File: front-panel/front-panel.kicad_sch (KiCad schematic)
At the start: 9 parts

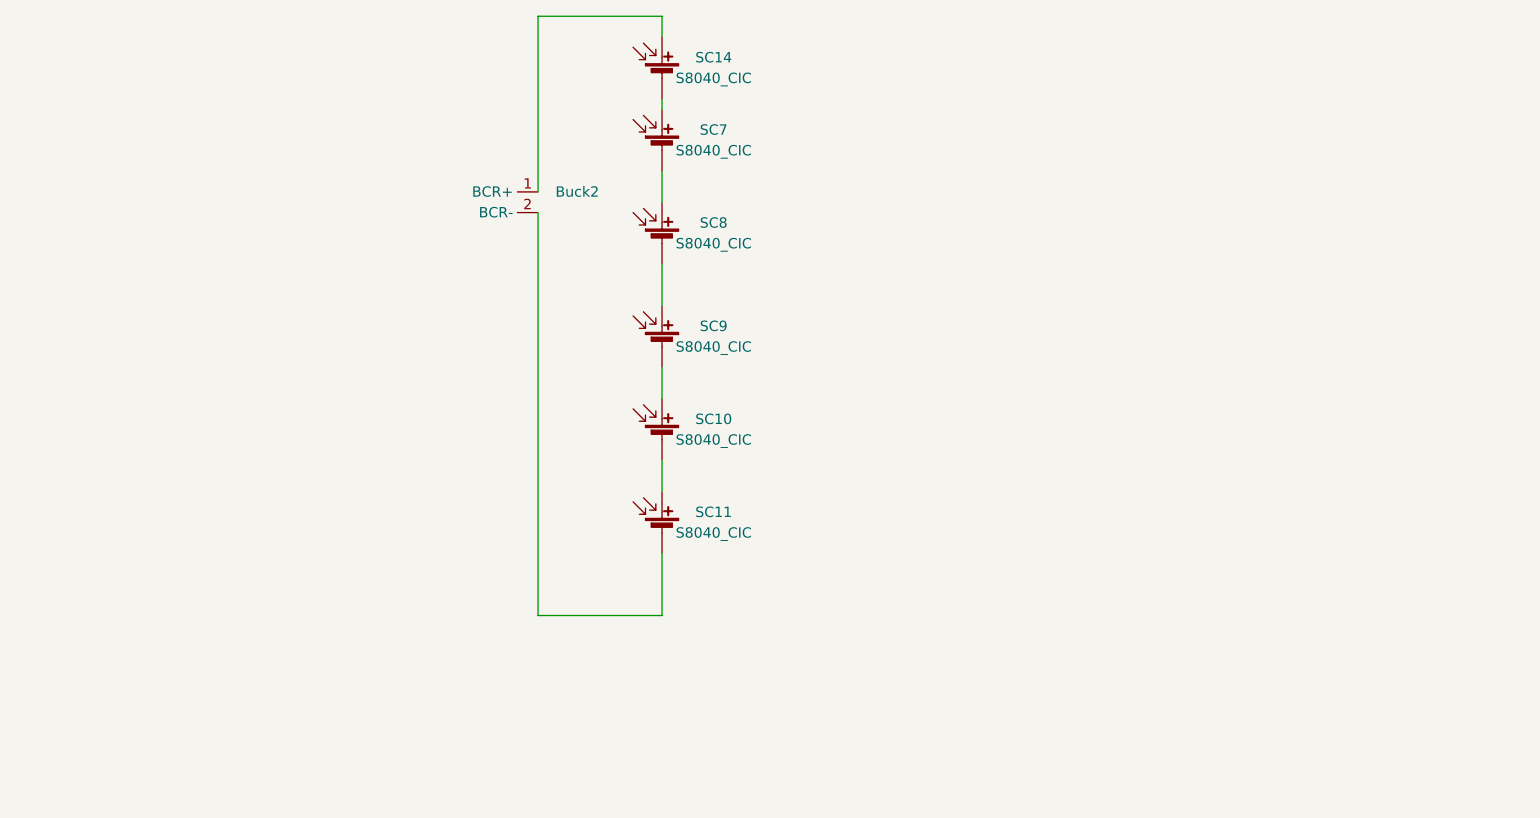
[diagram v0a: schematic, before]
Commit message: Added projects for blank PCBs, updated solar panels
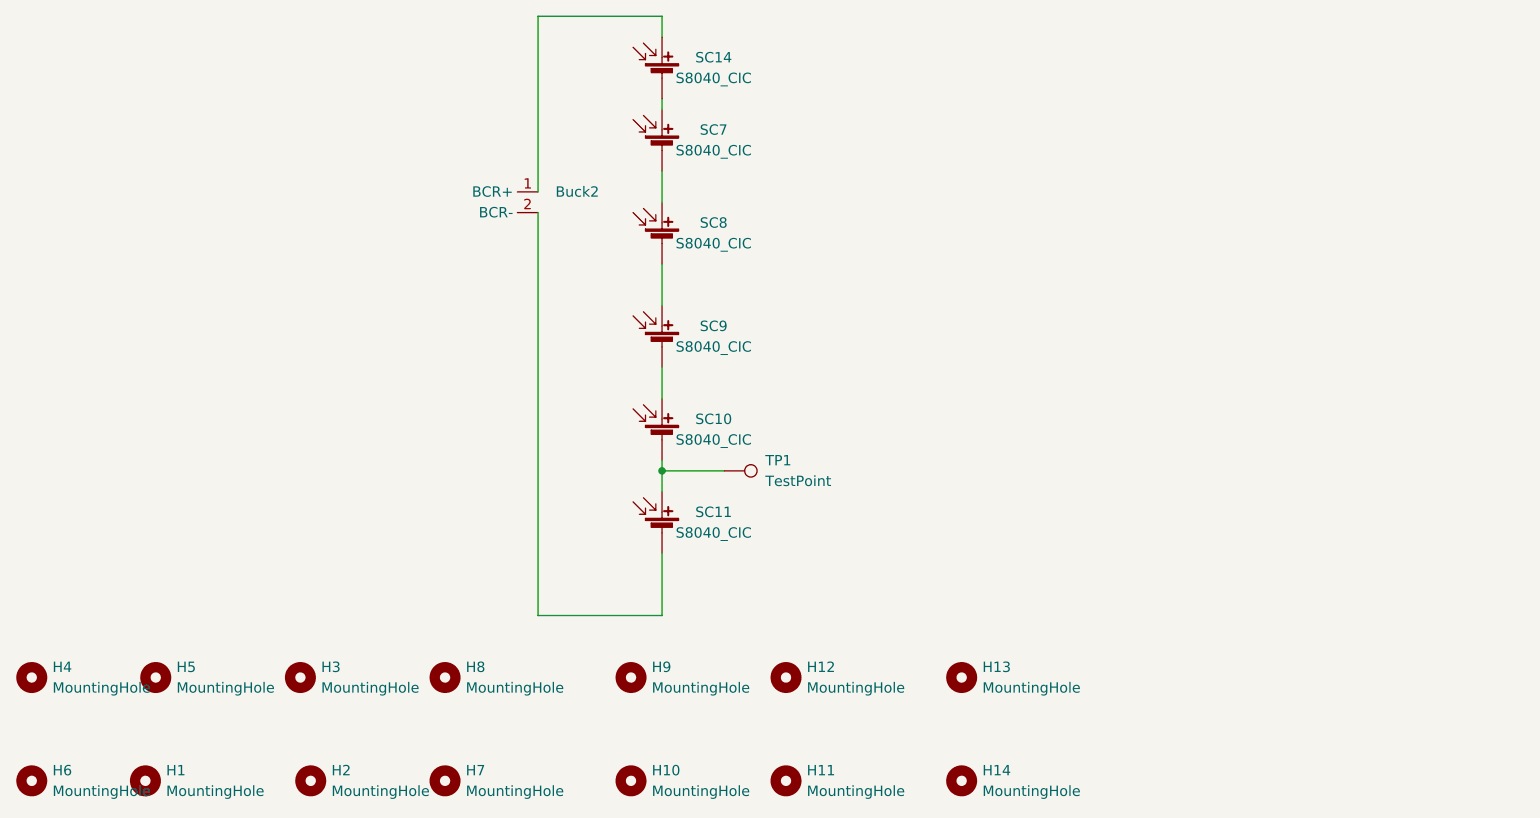
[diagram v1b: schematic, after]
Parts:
- added H1, H13, H14, H2, H3, H4, H5, H6, H7, H8: MountingHole, MountingHole:MountingHole_3.2mm_M3, symbol Mechanical:MountingHole
- added H10, H11, H12, H9: MountingHole, MountingHole:MountingHole_2.7mm, symbol Mechanical:MountingHole
- added TP1: TestPoint, TestPoint:TestPoint_Pad_D4.0mm, symbol Connector:TestPoint
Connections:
- net at SC10.2 (-), SC11.1 (+): now also TP1.1

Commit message: Removed GND and PWR plane, replaced with traces, switches are now in series rather than in parallel
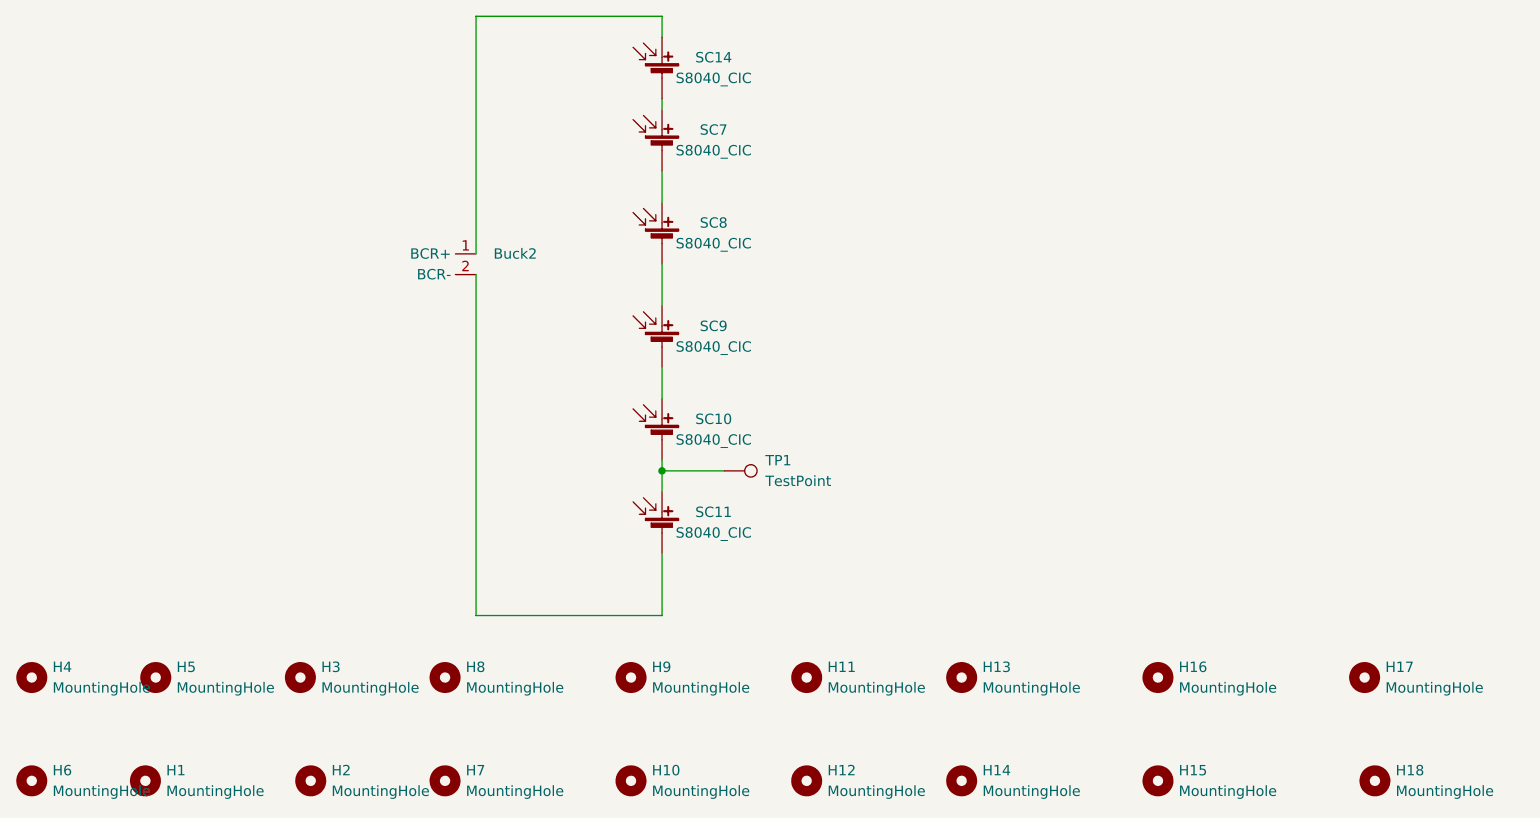
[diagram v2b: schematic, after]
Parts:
- added H15, H16, H17, H18: MountingHole, MountingHole:MountingHole_2.5mm, symbol Mechanical:MountingHole
- H10, H11, H12, H9: footprint MountingHole:MountingHole_2.7mm -> MountingHole:MountingHole_2.5mm
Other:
- moved on the sheet: Buck2
